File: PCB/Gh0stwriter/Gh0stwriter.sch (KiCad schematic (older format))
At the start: 2 parts

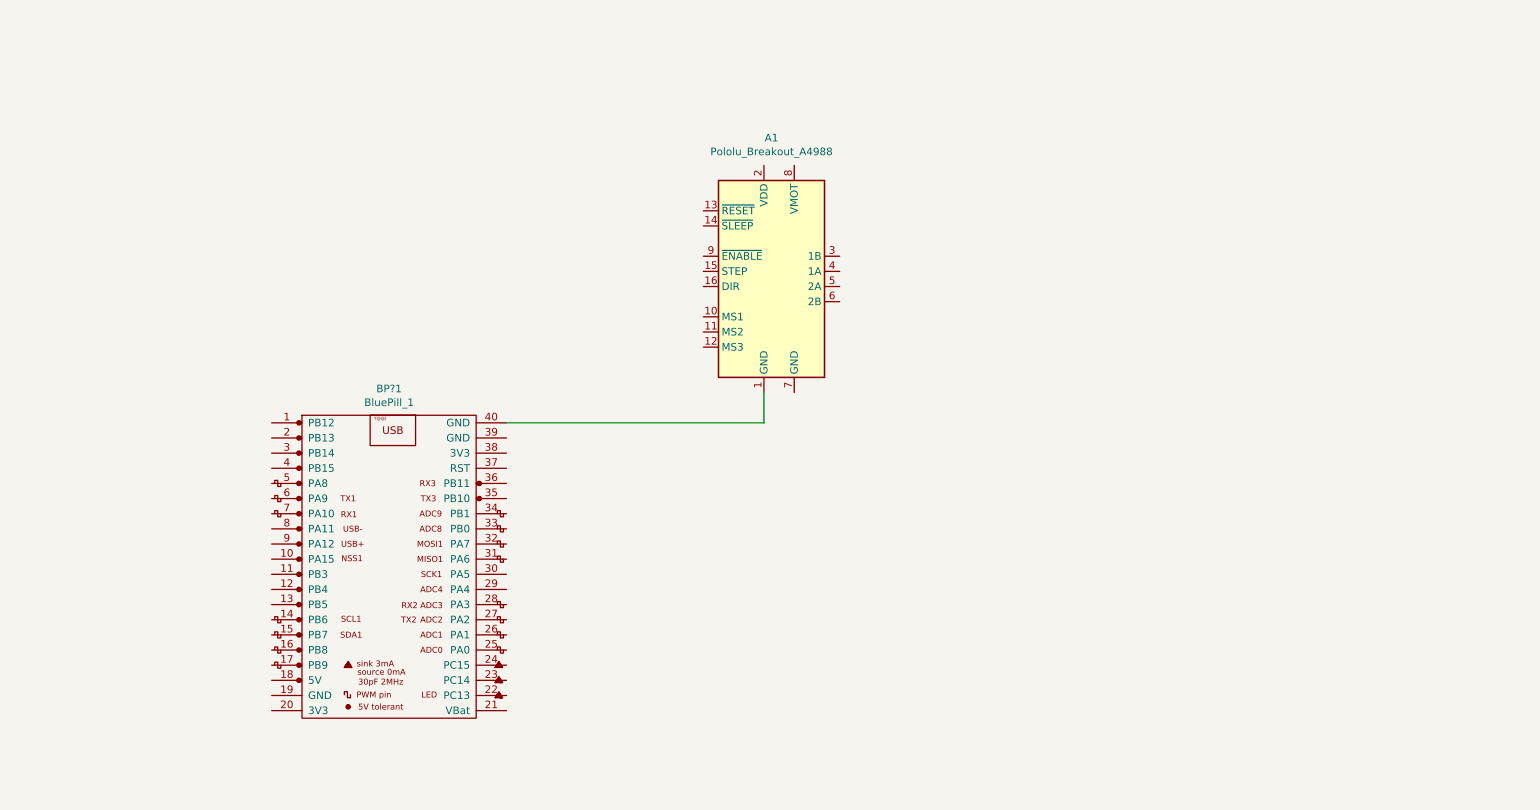
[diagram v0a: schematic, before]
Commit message: Created pcb outline
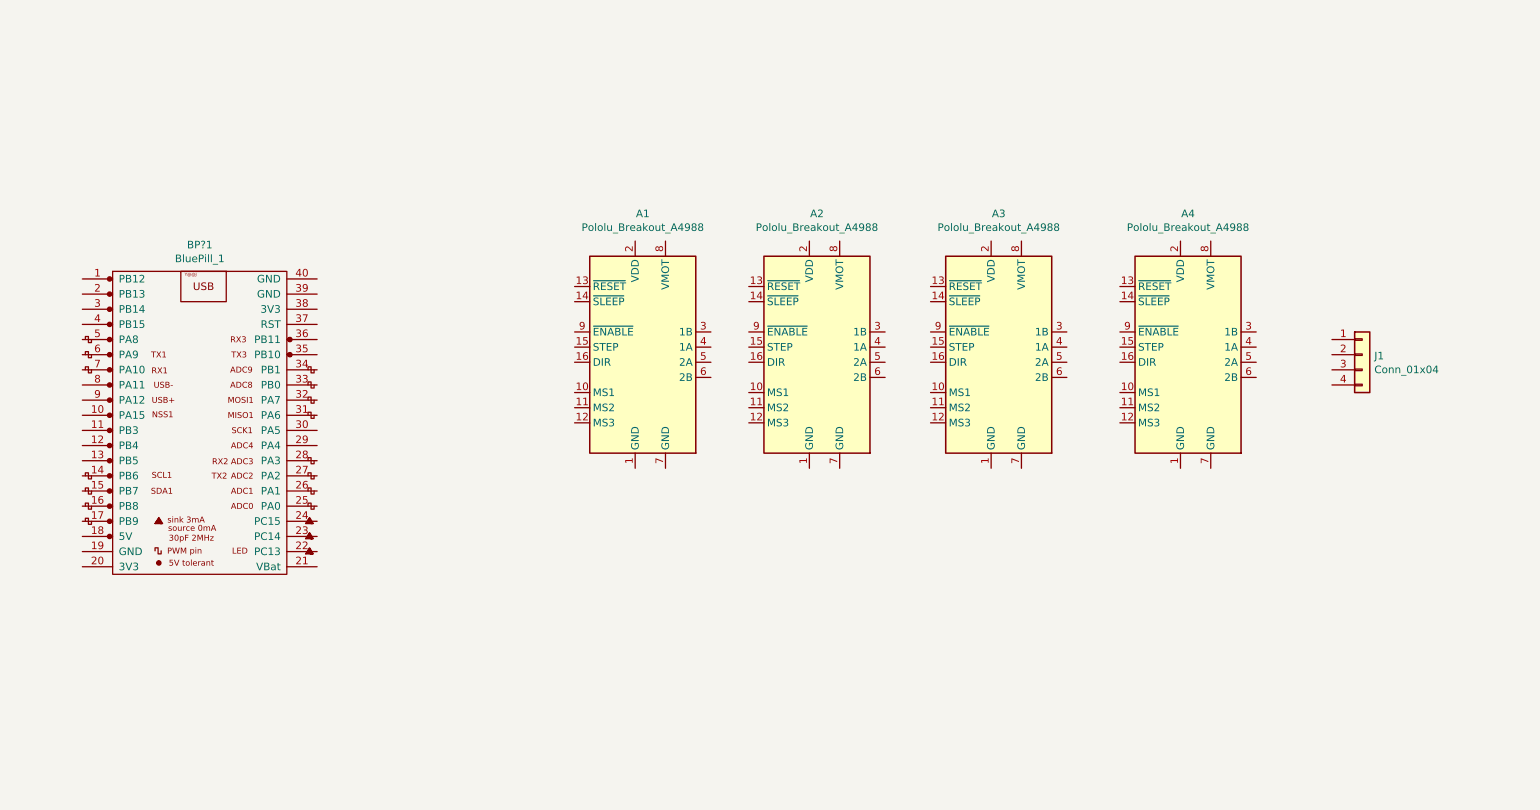
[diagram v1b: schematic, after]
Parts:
- added A1, A2, A4: Pololu_Breakout_A4988, Module:Pololu_Breakout-16_15.2x20.3mm, symbol Driver_Motor:Pololu_Breakout_A4988
- added J1: Conn_01x04, Connector_JST:JST_XH_B6B-XH-A_1x06_P2.50mm_Vertical, symbol Connector_Generic:Conn_01x04
- renumbered A1 to A3
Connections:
- net at A3.1 (GND): no longer BP?1.40 (GND)
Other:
- moved on the sheet: A3, BP?1
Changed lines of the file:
@@
 $EndDescr
 $Comp
-L Driver_Motor:Pololu_Breakout_A4988 A1
+L Driver_Motor:Pololu_Breakout_A4988 A3
 U 1 1 5ECE574D
-P 5650 3750
-F 0 "A1" H 5700 4631 50  0000 C CNN
-F 1 "Pololu_Breakout_A4988" H 5700 4540 50  0000 C CNN
-F 2 "Module:Pololu_Breakout-16_15.2x20.3mm" H 5925 3000 50  0001 L CNN
-F 3 "https://www.pololu.com/product/2980/pictures" H 5750 3450 50  0001 C CNN
-	1    5650 3750
+P 7150 4250
+F 0 "A3" H 7200 5131 50  0000 C CNN
+F 1 "Pololu_Breakout_A4988" H 7200 5040 50  0000 C CNN
+F 2 "Module:Pololu_Breakout-16_15.2x20.3mm" H 7425 3500 50  0001 L CNN
+F 3 "https://www.pololu.com/product/2980/pictures" H 7250 3950 50  0001 C CNN
+	1    7150 4250
 	1    0    0    -1
 $EndComp
@@
 L YAAJ_STM32:BluePill_1 BP?1
 U 1 1 5ECE59A4
-P 2600 4700
-F 0 "BP?1" H 3175 4875 50  0000 C CNN
-F 1 "BluePill_1" H 3175 4784 50  0000 C CNN
-F 2 "bluepill:YAAJ_BluePill" H 3850 2750 50  0001 C CNN
-F 3 "" H 3850 2750 50  0001 C CNN
-	1    2600 4700
+P 1350 3750
+F 0 "BP?1" H 1925 3925 50  0000 C CNN
+F 1 "BluePill_1" H 1925 3834 50  0000 C CNN
+F 2 "bluepill:YAAJ_BluePill" H 2600 1800 50  0001 C CNN
+F 3 "" H 2600 1800 50  0001 C CNN
+	1    1350 3750
 	1    0    0    -1
 $EndComp
-Wire Wire Line
-	3950 4750 5650 4750
-Wire Wire Line
-	5650 4750 5650 4550
+$Comp
+L Driver_Motor:Pololu_Breakout_A4988 A4
+U 1 1 5ECF26AB
+P 8400 4250
+F 0 "A4" H 8450 5131 50  0000 C CNN
+F 1 "Pololu_Breakout_A4988" H 8450 5040 50  0000 C CNN
+F 2 "Module:Pololu_Breakout-16_15.2x20.3mm" H 8675 3500 50  0001 L CNN
+F 3 "https://www.pololu.com/product/2980/pictures" H 8500 3950 50  0001 C CNN
+	1    8400 4250
+	1    0    0    -1
+$EndComp
+$Comp
+L Driver_Motor:Pololu_Breakout_A4988 A1
+U 1 1 5ECFA6A8
+P 4800 4250
+F 0 "A1" H 4850 5131 50  0000 C CNN
+F 1 "Pololu_Breakout_A4988" H 4850 5040 50  0000 C CNN
+F 2 "Module:Pololu_Breakout-16_15.2x20.3mm" H 5075 3500 50  0001 L CNN
+F 3 "https://www.pololu.com/product/2980/pictures" H 4900 3950 50  0001 C CNN
+	1    4800 4250
+	1    0    0    -1
+$EndComp
+$Comp
+L Driver_Motor:Pololu_Breakout_A4988 A2
+U 1 1 5ECFA6AE
+P 5950 4250
+F 0 "A2" H 6000 5131 50  0000 C CNN
+F 1 "Pololu_Breakout_A4988" H 6000 5040 50  0000 C CNN
+F 2 "Module:Pololu_Breakout-16_15.2x20.3mm" H 6225 3500 50  0001 L CNN
+F 3 "https://www.pololu.com/product/2980/pictures" H 6050 3950 50  0001 C CNN
+	1    5950 4250
+	1    0    0    -1
+$EndComp
+$Comp
+L Connector_Generic:Conn_01x04 J1
+U 1 1 5ED03F38
+P 9600 4300
+F 0 "J1" H 9680 4292 50  0000 L CNN
+F 1 "Conn_01x04" H 9680 4201 50  0000 L CNN
+F 2 "Connector_JST:JST_XH_B6B-XH-A_1x06_P2.50mm_Vertical" H 9600 4300 50  0001 C CNN
+F 3 "~" H 9600 4300 50  0001 C CNN
+	1    9600 4300
+	1    0    0    -1
+$EndComp
 $EndSCHEMATC

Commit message: Started routing
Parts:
- removed J1: Conn_01x04, Connector_JST:JST_XH_B6B-XH-A_1x06_P2.50mm_Vertical, symbol Connector_Generic:Conn_01x04
- added C1, C2: CP, Capacitor_THT:CP_Radial_D8.0mm_P2.50mm, symbol Device:CP
- added C3, C4: C, Capacitor_THT:C_Disc_D4.7mm_W2.5mm_P5.00mm, symbol Device:C
- added D1: 1N4007, Diode_THT:D_DO-41_SOD81_P10.16mm_Horizontal, symbol Diode:1N4007
- added J1, J3, J5, J6: Conn_01x06, Connector_JST:JST_XH_B6B-XH-A_1x06_P2.50mm_Vertical, symbol Connector_Generic:Conn_01x06
- added J2, J4: Conn_01x02, Connector_JST:JST_XH_B2B-XH-A_1x02_P2.50mm_Vertical, symbol Connector_Generic:Conn_01x02
- added J7: Conn_01x02, TerminalBlock_Phoenix:TerminalBlock_Phoenix_MKDS-1,5-2_1x02_P5.00mm_Horizontal, symbol Connector_Generic:Conn_01x02
- added Q1: Q_NPN_Darlington_ECB, Package_TO_SOT_THT:TO-126-3_Vertical, symbol Device:Q_NPN_Darlington_ECB
- added SerialPort1: Conn_01x06, Connector_PinHeader_2.54mm:PinHeader_1x06_P2.54mm_Vertical, symbol Connector_Generic:Conn_01x06
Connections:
- net GND: now reaches A3.1 (GND)
- net GND: now also A1.1 (GND), A1.7 (GND), A2.1 (GND), A2.7 (GND), A3.7 (GND), A4.1 (GND), A4.7 (GND), BP?1.19 (GND), BP?1.39 (GND), BP?1.40 (GND), C1.2, C2.2, C3.2, C4.2, J2.2 (Pin_2), J7.2 (Pin_2), Q1.1 (E), SerialPort1.6 (Pin_6)
- net ICReset: now reaches A3.13 (~RESET)
- net ICReset: now also A1.13 (~RESET), A2.13 (~RESET), A4.13 (~RESET), BP?1.1 (PB12)
- net +3V3: now reaches A3.2 (VDD)
- net +3V3: now also A1.2 (VDD), A2.2 (VDD), A4.2 (VDD), BP?1.20 (3V3), C1.1, C3.1
- net at A3.3 (1B): now also J5.3 (Pin_3)
- net at A3.4 (1A): now also J5.4 (Pin_4)
- net at A3.5 (2A): now also J5.5 (Pin_5)
- net at A3.6 (2B): now also J5.6 (Pin_6)
- net Vdrive: now reaches A3.8 (VMOT)
- net Vdrive: now also A1.8 (VMOT), A2.8 (VMOT), A4.8 (VMOT), C2.1, C4.1, D1.1 (K), J4.1 (Pin_1), J7.1 (Pin_1)
- net PA9: now reaches BP?1.6 (PA9)
- net PA9: now also SerialPort1.2 (Pin_2)
- net PA10: now reaches BP?1.7 (PA10)
- net PA10: now also SerialPort1.3 (Pin_3)
- net at A4.3 (1B): now also J6.3 (Pin_3)
- net at A4.4 (1A): now also J6.4 (Pin_4)
- net at A4.5 (2A): now also J6.5 (Pin_5)
- net at A4.6 (2B): now also J6.6 (Pin_6)
- net at A1.3 (1B): now also J1.3 (Pin_3)
- net at A1.4 (1A): now also J1.4 (Pin_4)
- net at A1.5 (2A): now also J1.5 (Pin_5)
- net at A1.6 (2B): now also J1.6 (Pin_6)
- net at A2.3 (1B): now also J3.3 (Pin_3)
- net at A2.4 (1A): now also J3.4 (Pin_4)
- net at A2.5 (2A): now also J3.5 (Pin_5)
- net at A2.6 (2B): now also J3.6 (Pin_6)
- new net: D1.2 (A), J4.2 (Pin_2), Q1.2 (C)
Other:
- moved on the sheet: A1, A2, A3, A4
